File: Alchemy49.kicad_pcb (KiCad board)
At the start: 2 copper layers, 267.5 x 76.2 mm, 205 parts, among them J1 USB_B_Micro, J2 Conn_01x05_Female, Q1 2N7002E, SW1 ESC-1.5U, SW10 O-1U, SW11 P-1U, SW12 BACK-1.5U, SW13 DEL-1U, SW14 TAB-1.75U, SW15 A-1U, SW16 S-1U, SW17 D-1U, SW18 F-1U, SW19 G-1U, SW2 Q-1U, SW20 H-1U, SW21 J-1U, SW22 K-1U, SW23 L-1U, SW24 ENTER-2.25U, SW25 PGUP-1U, SW26 SHIFT-2U, SW27 Z-1U, SW28 X-1U, SW29 C-1U, SW3 W-1U, SW30 V-1U, SW31 B-1U, SW32 N-1U, SW33 M-1U, SW34 COM-1U, SW35 PER-1U, SW36 SLASH-1U, SW37 UP-1U, SW38 PGDN-1U, SW39 CTRL1-1U, SW4 E-1U, SW40 WIN-1U, SW41 ALT-1U, SW42 FN1-1U, SW43 SPACE-2.75U, SW44 SHIFT-2.25U, SW45 FN2-1U, SW46 CTRL2-1U, SW47 LEFT-1U, SW48 DOWN-1U, SW49 RIGHT-1U, SW5 R-1U, SW6 T-1U, SW7 Y-1U, SW8 U-1U, SW9 I-1U

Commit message: Added Switch Silkscreen Outlines
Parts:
- added ,: Switch SilkS, Alchemy49:Switch SilkS, F.Cu at (195.3, 61.1)
- added .: Switch SilkS, Alchemy49:Switch SilkS, F.Cu at (214.3, 61.1)
- added /: Switch SilkS, Alchemy49:Switch SilkS, F.Cu at (233.4, 61.1)
- added A: Switch SilkS, Alchemy49:Switch SilkS, F.Cu at (57.1, 42.1)
- added ALT: Switch SilkS, Alchemy49:Switch SilkS, F.Cu at (61.9, 80.2)
- added B: Switch SilkS, Alchemy49:Switch SilkS, F.Cu at (138.1, 61.1)
- added BACK: Switch SilkS, Alchemy49:Switch SilkS, F.Cu at (247.7, 23.0)
- added C: Switch SilkS, Alchemy49:Switch SilkS, F.Cu at (100.0, 61.1)
- added CTRL: Switch SilkS, Alchemy49:Switch SilkS, F.Cu at (214.3, 80.2)
- added CTRL: Switch SilkS, Alchemy49:Switch SilkS, F.Cu at (23.8, 80.2)
- added D: Switch SilkS, Alchemy49:Switch SilkS, F.Cu at (95.2, 42.1)
- added DEL: Switch SilkS, Alchemy49:Switch SilkS, F.Cu at (271.5, 23.0)
- added E: Switch SilkS, Alchemy49:Switch SilkS, F.Cu at (90.5, 23.0)
- added ENTER: Switch SilkS, Alchemy49:Switch SilkS, F.Cu at (240.5, 42.1)
- added ESC: Switch SilkS, Alchemy49:Switch SilkS, F.Cu at (28.6, 23.0)
- added F: Switch SilkS, Alchemy49:Switch SilkS, F.Cu at (114.3, 42.1)
- added FN: Switch SilkS, Alchemy49:Switch SilkS, F.Cu at (195.3, 80.2)
- added FN: Switch SilkS, Alchemy49:Switch SilkS, F.Cu at (81.0, 80.2)
- added G: Switch SilkS, Alchemy49:Switch SilkS, F.Cu at (133.3, 42.1)
- added H: Switch SilkS, Alchemy49:Switch SilkS, F.Cu at (152.4, 42.1)
- added I: Switch SilkS, Alchemy49:Switch SilkS, F.Cu at (185.7, 23.0)
- added J: Switch SilkS, Alchemy49:Switch SilkS, F.Cu at (171.4, 42.1)
- added K: Switch SilkS, Alchemy49:Switch SilkS, F.Cu at (190.5, 42.1)
- added L: Switch SilkS, Alchemy49:Switch SilkS, F.Cu at (209.6, 42.1)
- added M: Switch SilkS, Alchemy49:Switch SilkS, F.Cu at (176.2, 61.1)
- added N: Switch SilkS, Alchemy49:Switch SilkS, F.Cu at (157.2, 61.1)
- added O: Switch SilkS, Alchemy49:Switch SilkS, F.Cu at (204.8, 23.0)
- added P: Switch SilkS, Alchemy49:Switch SilkS, F.Cu at (223.8, 23.0)
- added PGDN: Switch SilkS, Alchemy49:Switch SilkS, F.Cu at (271.5, 61.1)
- added PGUP: Switch SilkS, Alchemy49:Switch SilkS, F.Cu at (271.5, 42.1)
- added Q: Switch SilkS, Alchemy49:Switch SilkS, F.Cu at (52.4, 23.0)
- added R: Switch SilkS, Alchemy49:Switch SilkS, F.Cu at (109.5, 23.0)
- added S: Switch SilkS, Alchemy49:Switch SilkS, F.Cu at (76.2, 42.1)
- added SHIFT: Switch SilkS, Alchemy49:Switch SilkS, F.Cu at (164.3, 80.2)
- added SHIFT: Switch SilkS, Alchemy49:Switch SilkS, F.Cu at (33.3, 61.1)
- added SPACE: Switch SilkS, Alchemy49:Switch SilkS, F.Cu at (116.7, 80.2)
- added T: Switch SilkS, Alchemy49:Switch SilkS, F.Cu at (128.6, 23.0)
- added TAB: Switch SilkS, Alchemy49:Switch SilkS, F.Cu at (31.0, 42.1)
- added U: Switch SilkS, Alchemy49:Switch SilkS, F.Cu at (166.7, 23.0)
- added V: Switch SilkS, Alchemy49:Switch SilkS, F.Cu at (119.1, 61.1)
- added W: Switch SilkS, Alchemy49:Switch SilkS, F.Cu at (71.4, 23.0)
- added WIN: Switch SilkS, Alchemy49:Switch SilkS, F.Cu at (42.9, 80.2)
- added X: Switch SilkS, Alchemy49:Switch SilkS, F.Cu at (81.0, 61.1)
- added Y: Switch SilkS, Alchemy49:Switch SilkS, F.Cu at (147.6, 23.0)
- added Z: Switch SilkS, Alchemy49:Switch SilkS, F.Cu at (61.9, 61.1)
- added ←: Switch SilkS, Alchemy49:Switch SilkS, F.Cu at (271.5, 80.2)
- added ↑: Switch SilkS, Alchemy49:Switch SilkS, F.Cu at (252.4, 61.1)
- added →: Switch SilkS, Alchemy49:Switch SilkS, F.Cu at (233.4, 80.2)
- added ↓: Switch SilkS, Alchemy49:Switch SilkS, F.Cu at (252.4, 80.2)
- moved R50 15.2 mm to (137.2, 70.6), turned to 180 degrees
- moved R51 11.5 mm to (137.2, 72.7), turned to 0 degrees
- moved Q1 8.46 mm to (149.8, 66.6)
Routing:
- net LED: track 889.5 -> 881.1 mm
- net Net-(Q1-Pad1): track 9.27 -> 17.2 mm
- net Row4: track 267.8 -> 273.5 mm
- net LEDCTL: track 36.2 -> 34.4 mm

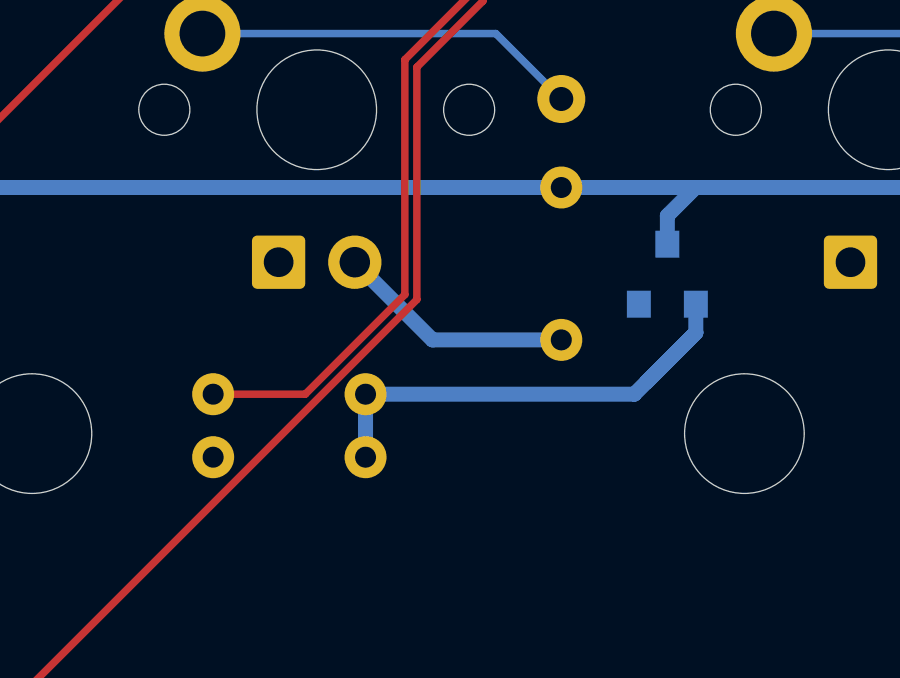
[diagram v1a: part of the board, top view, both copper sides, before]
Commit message: Adjusted MOSFET location
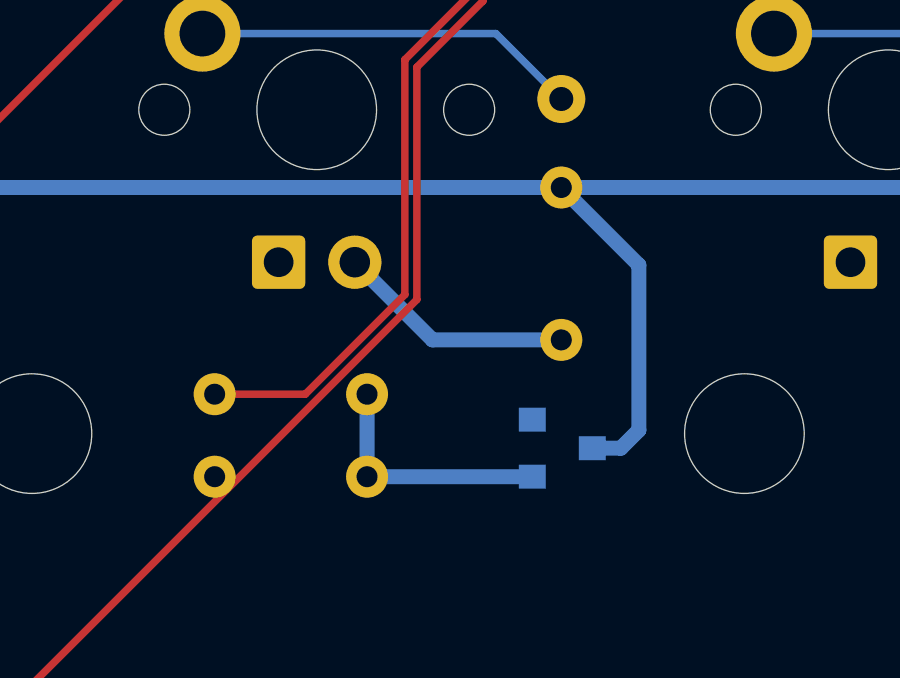
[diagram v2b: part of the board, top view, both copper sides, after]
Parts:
- moved Q1 6.77 mm to (146.3, 72.4), turned to 0 degrees
- moved R51 0.65 mm to (137.2, 73.3)
- moved R50 0.05 mm to (137.2, 70.6)
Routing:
- net Net-(Q1-Pad1): track 17.2 -> 8.26 mm
- net LED: track 881.1 -> 889.8 mm
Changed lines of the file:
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@@
     (thickness 1.6)
     (drawings 24)
-    (tracks 832)
+    (tracks 831)
     (zones 0)
     (modules 254)
@@
   )
   (setup
-    (last_trace_width 0.5)
+    (last_trace_width 0.25)
     (user_trace_width 0.1)
     (user_trace_width 0.2)
@@
   )
   (module Package_TO_SOT_SMD:SOT-23 (layer B.Cu)
-    (at 149.8 66.6 90)
+    (at 146.3 72.4)
     (descr "SOT-23, Standard")
     (tags SOT-23)
     (attr smd)
-    (fp_text reference Q1 (at -0.1 0 180) (layer B.SilkS)
+    (fp_text reference Q1 (at -0.1 0 270) (layer B.SilkS)
       (effects (font (size 0.75 0.75) (thickness 0.15)) (justify mirror))
     )
-    (fp_text value 2N7002E (at 0 -2.5 90) (layer B.Fab)
+    (fp_text value 2N7002E (at 0 -2.5) (layer B.Fab)
       (effects (font (size 1 1) (thickness 0.15)) (justify mirror))
     )
@@
     (fp_line (start -0.15 1.52) (end 0.7 1.52) (layer B.Fab) (width 0.1))
     (fp_line (start -0.7 0.95) (end -0.7 -1.5) (layer B.Fab) (width 0.1))
-    (fp_text user %R (at 0 0 180) (layer B.Fab)
+    (fp_text user %R (at 0 0 270) (layer B.Fab)
       (effects (font (size 0.5 0.5) (thickness 0.075)) (justify mirror))
     )
-    (pad 3 smd rect (at 1 0 90) (size 0.9 0.8) (layers B.Cu B.Paste B.Mask)
+    (pad 3 smd rect (at 1 0) (size 0.9 0.8) (layers B.Cu B.Paste B.Mask)
       (net 124 LED))
-    (pad 2 smd rect (at -1 -0.95 90) (size 0.9 0.8) (layers B.Cu B.Paste B.Mask)
+    (pad 2 smd rect (at -1 -0.95) (size 0.9 0.8) (layers B.Cu B.Paste B.Mask)
       (net 70 GND))
-    (pad 1 smd rect (at -1 0.95 90) (size 0.9 0.8) (layers B.Cu B.Paste B.Mask)
+    (pad 1 smd rect (at -1 0.95) (size 0.9 0.8) (layers B.Cu B.Paste B.Mask)
       (net 126 "Net-(Q1-Pad1)"))
     (model ${KISYS3DMOD}/Package_TO_SOT_SMD.3dshapes/SOT-23.wrl
@@
   )
   (module AcheronLibrary_COM:R_THT_5.08mm_Horizontal (layer B.Cu)
-    (at 137.2 70.6 180)
+    (at 137.25 70.6 180)
     (descr "Resistor, Axial_DIN0204 series, Axial, Horizontal, pin pitch=5.08mm, 0.167W, length*diameter=3.6*1.6mm^2, http://cdn-reichelt.de/documents/datenblatt/B400/1_4W%23YAG.pdf")
     (tags "Resistor Axial_DIN0204 series Axial Horizontal pin pitch 5.08mm 0.167W length 3.6mm diameter 1.6mm")
@@
   )
   (module AcheronLibrary_COM:R_THT_5.08mm_Horizontal (layer B.Cu)
-    (at 137.2 72.7)
+    (at 137.25 73.35)
     (descr "Resistor, Axial_DIN0204 series, Axial, Horizontal, pin pitch=5.08mm, 0.167W, length*diameter=3.6*1.6mm^2, http://cdn-reichelt.de/documents/datenblatt/B400/1_4W%23YAG.pdf")
     (tags "Resistor Axial_DIN0204 series Axial Horizontal pin pitch 5.08mm 0.167W length 3.6mm diameter 1.6mm")
@@
   (segment (start 30.015 37.14374) (end 31.87126 39) (width 0.5) (layer B.Cu) (net 124))
   (segment (start 150.74 63.71) (end 151.96 63.71) (width 0.5) (layer B.Cu) (net 124))
-  (segment (start 149.8 64.65) (end 150.74 63.71) (width 0.5) (layer B.Cu) (net 124))
-  (segment (start 149.8 65.6) (end 149.8 64.65) (width 0.5) (layer B.Cu) (net 124))
+  (segment (start 148.85 66.295) (end 146.265 63.71) (width 0.5) (layer B.Cu) (net 124))
+  (segment (start 148.85 71.8) (end 148.85 66.295) (width 0.5) (layer B.Cu) (net 124))
+  (segment (start 148.25 72.4) (end 148.85 71.8) (width 0.5) (layer B.Cu) (net 124))
+  (segment (start 147.3 72.4) (end 148.25 72.4) (width 0.5) (layer B.Cu) (net 124))
   (segment (start 137.7313 70.6) (end 134.66 70.6) (width 0.25) (layer F.Cu) (net 125))
   (segment (start 141.04999 67.28131) (end 137.7313 70.6) (width 0.25) (layer F.Cu) (net 125))
@@
   (segment (start 143.895199 50.049102) (end 143.24999 50.694311) (width 0.25) (layer F.Cu) (net 125))
   (segment (start 143.24999 50.694311) (end 143.24999 57.25001) (width 0.25) (layer F.Cu) (net 125))
-  (segment (start 150.75 68.55) (end 150.75 67.6) (width 0.5) (layer B.Cu) (net 126))
-  (segment (start 149.1 70.2) (end 150.75 68.55) (width 0.5) (layer B.Cu) (net 126))
-  (segment (start 148.7 70.6) (end 150.75 68.55) (width 0.5) (layer B.Cu) (net 126))
-  (segment (start 139.74 70.6) (end 148.7 70.6) (width 0.5) (layer B.Cu) (net 126))
-  (segment (start 139.74 72.7) (end 139.74 70.6) (width 0.5) (layer B.Cu) (net 126))
+  (segment (start 145.3 73.35) (end 139.79 73.35) (width 0.5) (layer B.Cu) (net 126))
+  (segment (start 139.79 70.6) (end 139.79 73.35) (width 0.5) (layer B.Cu) (net 126))
   (segment (start 40 29.45) (end 40 28.8672) (width 0.25) (layer B.Cu) (net 127))
   (segment (start 39.992479 29.516756) (end 40 29.45) (width 0.25) (layer B.Cu) (net 127))

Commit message: Added Bottom Silk Screen
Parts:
- added REF**: Logo, Alchemy49:Logo, B.Cu at (139.9, 77.6)

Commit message: Finalized Board Design
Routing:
- net Row4: track 273.5 -> 255.8 mm
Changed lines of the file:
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@@
     (thickness 1.6)
     (drawings 24)
-    (tracks 831)
+    (tracks 827)
     (zones 0)
     (modules 255)
@@
   (segment (start 206.16 72.19) (end 225.21 72.19) (width 0.25) (layer B.Cu) (net 8))
   (segment (start 225.21 72.19) (end 241.515 72.19) (width 0.25) (layer B.Cu) (net 8))
-  (segment (start 136.1 87.1) (end 132.3 83.3) (width 0.25) (layer F.Cu) (net 8))
-  (segment (start 184.365 72.19) (end 169.355 87.2) (width 0.25) (layer F.Cu) (net 8))
-  (segment (start 169.355 87.2) (end 157.25 87.2) (width 0.25) (layer F.Cu) (net 8))
-  (segment (start 157.25 87.2) (end 153.95 83.9) (width 0.25) (layer F.Cu) (net 8))
-  (segment (start 153.95 83.9) (end 151.2 83.9) (width 0.25) (layer F.Cu) (net 8))
-  (segment (start 151.2 83.9) (end 148 87.1) (width 0.25) (layer F.Cu) (net 8))
-  (segment (start 148 87.1) (end 136.1 87.1) (width 0.25) (layer F.Cu) (net 8))
-  (segment (start 130.35 83.3) (end 132.3 83.3) (width 0.25) (layer F.Cu) (net 8))
   (segment (start 34.49 71.59) (end 35.09 72.19) (width 0.25) (layer B.Cu) (net 8))
   (segment (start 31.965 71.59) (end 34.49 71.59) (width 0.25) (layer B.Cu) (net 8))
   (segment (start 35.09 72.19) (end 50.115 72.19) (width 0.25) (layer B.Cu) (net 8))
   (segment (start 91.86 72.19) (end 102.97 83.3) (width 0.25) (layer F.Cu) (net 8))
-  (segment (start 102.97 83.3) (end 107.825 83.3) (width 0.25) (layer F.Cu) (net 8))
-  (segment (start 125.596999 83.3) (end 121.9 83.3) (width 0.25) (layer F.Cu) (net 8))
-  (segment (start 121.9 83.3) (end 130.35 83.3) (width 0.25) (layer F.Cu) (net 8))
-  (segment (start 107.825 83.3) (end 121.9 83.3) (width 0.25) (layer F.Cu) (net 8))
+  (segment (start 137.89699 77.70301) (end 132.3 83.3) (width 0.25) (layer F.Cu) (net 8))
+  (segment (start 141.45 74.15) (end 137.89699 77.70301) (width 0.25) (layer F.Cu) (net 8))
+  (segment (start 143.65 57.5) (end 141.45 59.7) (width 0.25) (layer F.Cu) (net 8))
   (segment (start 145.14 49.37) (end 143.65 50.86) (width 0.25) (layer F.Cu) (net 8))
   (segment (start 143.65 50.86) (end 143.65 57.5) (width 0.25) (layer F.Cu) (net 8))
-  (segment (start 141.45 67.446999) (end 125.596999 83.3) (width 0.25) (layer F.Cu) (net 8))
-  (segment (start 143.65 57.5) (end 141.45 59.7) (width 0.25) (layer F.Cu) (net 8))
-  (segment (start 141.45 59.7) (end 141.45 67.446999) (width 0.25) (layer F.Cu) (net 8))
+  (segment (start 102.97 83.3) (end 132.3 83.3) (width 0.25) (layer F.Cu) (net 8))
+  (segment (start 141.45 72.79) (end 141.45 74.15) (width 0.25) (layer F.Cu) (net 8))
+  (segment (start 141.45 67.35) (end 141.45 72.79) (width 0.25) (layer F.Cu) (net 8))
+  (segment (start 141.45 59.7) (end 141.45 67.35) (width 0.25) (layer F.Cu) (net 8))
+  (segment (start 141.46 74.15) (end 141.45 74.15) (width 0.25) (layer F.Cu) (net 8))
+  (segment (start 150.62 83.31) (end 141.46 74.15) (width 0.25) (layer F.Cu) (net 8))
+  (segment (start 184.365 72.19) (end 173.245 83.31) (width 0.25) (layer F.Cu) (net 8))
+  (segment (start 173.245 83.31) (end 150.62 83.31) (width 0.25) (layer F.Cu) (net 8))
   (segment (start 103.56625 20.47875) (end 105.7275 20.47875) (width 0.25) (layer B.Cu) (net 9))
   (segment (start 101.385 22.66) (end 103.56625 20.47875) (width 0.25) (layer B.Cu) (net 9))
@@
   (segment (start 148.25 72.4) (end 148.85 71.8) (width 0.5) (layer B.Cu) (net 124))
   (segment (start 147.3 72.4) (end 148.25 72.4) (width 0.5) (layer B.Cu) (net 124))
-  (segment (start 137.7313 70.6) (end 134.66 70.6) (width 0.25) (layer F.Cu) (net 125))
-  (segment (start 141.04999 67.28131) (end 137.7313 70.6) (width 0.25) (layer F.Cu) (net 125))
-  (segment (start 141.04999 59.45001) (end 141.04999 67.28131) (width 0.25) (layer F.Cu) (net 125))
   (segment (start 143.24999 57.25001) (end 141.04999 59.45001) (width 0.25) (layer F.Cu) (net 125))
   (segment (start 148.975199 48.225199) (end 144.526895 48.225199) (width 0.25) (layer F.Cu) (net 125))
@@
   (segment (start 143.895199 50.049102) (end 143.24999 50.694311) (width 0.25) (layer F.Cu) (net 125))
   (segment (start 143.24999 50.694311) (end 143.24999 57.25001) (width 0.25) (layer F.Cu) (net 125))
+  (segment (start 141.04999 59.45001) (end 141.04999 66.83001) (width 0.25) (layer F.Cu) (net 125))
+  (segment (start 137.28 70.6) (end 141.04999 66.83001) (width 0.25) (layer F.Cu) (net 125))
+  (segment (start 134.71 70.6) (end 137.28 70.6) (width 0.25) (layer F.Cu) (net 125))
   (segment (start 145.3 73.35) (end 139.79 73.35) (width 0.5) (layer B.Cu) (net 126))
   (segment (start 139.79 70.6) (end 139.79 73.35) (width 0.5) (layer B.Cu) (net 126))
